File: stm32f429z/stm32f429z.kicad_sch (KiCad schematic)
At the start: 1 part, among them U1 STM32F429ZITx

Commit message: finished schematics and mostly finished the routing for the pcb
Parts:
- added C22: 100n, Capacitor_SMD:C_0603_1608Metric_Pad1.08x0.95mm_HandSolder, symbol Device:C
- added H1, H2, H3, H4: MountingHole, MountingHole:MountingHole_4.3mm_M4_Pad_Via, symbol Mechanical:MountingHole
- added SW1: Boot0, Button_Switch_SMD:SW_SPDT_CK-JS102011SAQN, symbol Switch:SW_SPDT
- added SW2: NRST, Button_Switch_SMD:SW_SPST_PTS645, symbol Switch:SW_Push
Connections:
- net +3.3V: now also U1.143 (PDR_ON), SW1.2 (B)
- net +3.3VA: now also U1.32 (VREF+)
- net CAN2_TX: no longer U1.114 (PD0)
- net GND: now also C22.2, SW1.3 (C), SW2.1
- net CAN SIlent Mode 1: now reaches U1.116 (PD2)
- net SPI3_CS  : now reaches U1.124 (PG9)
- net SYS_JTDO-SWO: now reaches U1.133 (PB3)
- net BOOT0: now reaches U1.138 (BOOT0)
- net BOOT0: now also SW1.1 (A)
- net NRST: now reaches U1.25 (NRST)
- net NRST: now also C22.1, SW2.2
- net CAN SIlent Mode 2: now reaches U1.76 (PB15)
- net USB_OTG_FS_DM renamed USB_OTG_FS_DP-
- net USB_OTG_FS_DP renamed USB_OTG_FS_DP+
- net USB_OTG_FS_ID: no longer names the net of U1.102 (PA10)
- net USB_OTG_FS_VBUS: no longer names the net of U1.101 (PA9)
- new net CAN1_RX: U1.114 (PD0)
- no-connect marks 0 -> 81
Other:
- removed sheet I2C
- removed sheet SPI
- removed sheet adc
- added sheet connectors (connectors.kicad_sch)

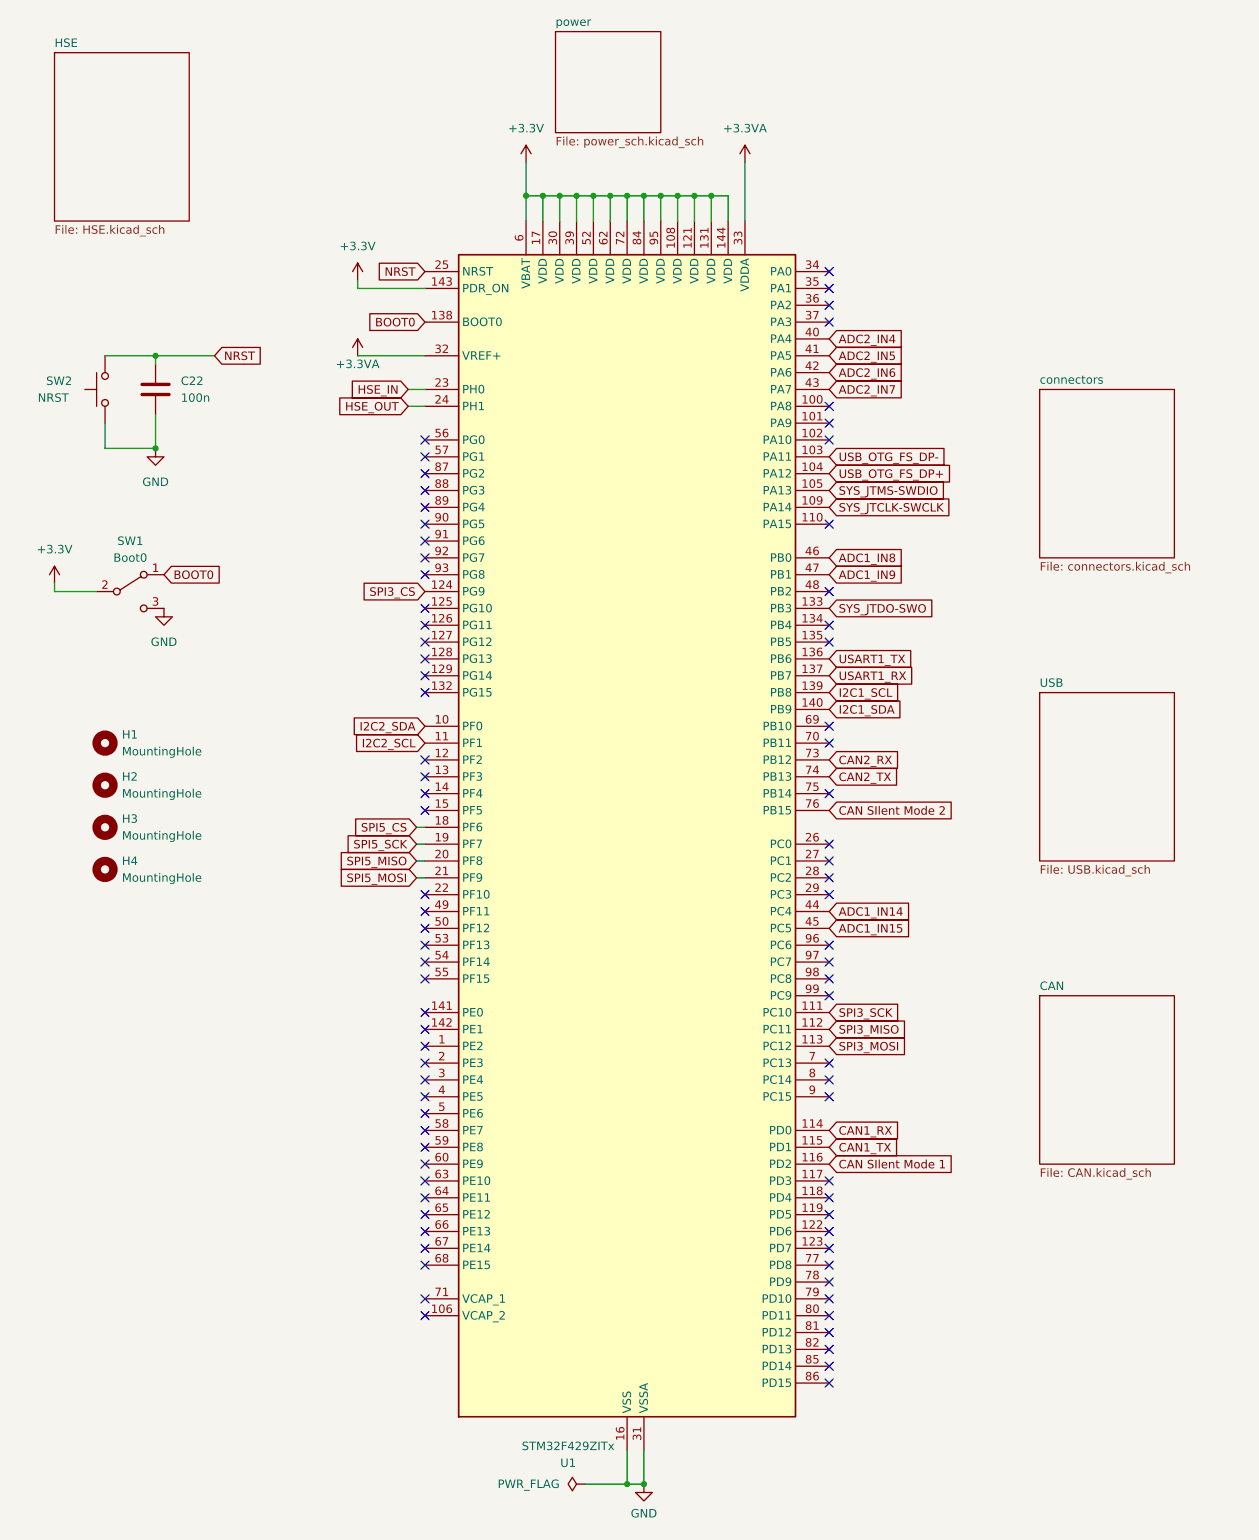
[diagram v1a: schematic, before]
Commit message: removed alot of the silk screen, changed oscillator foor print and added GPIOs
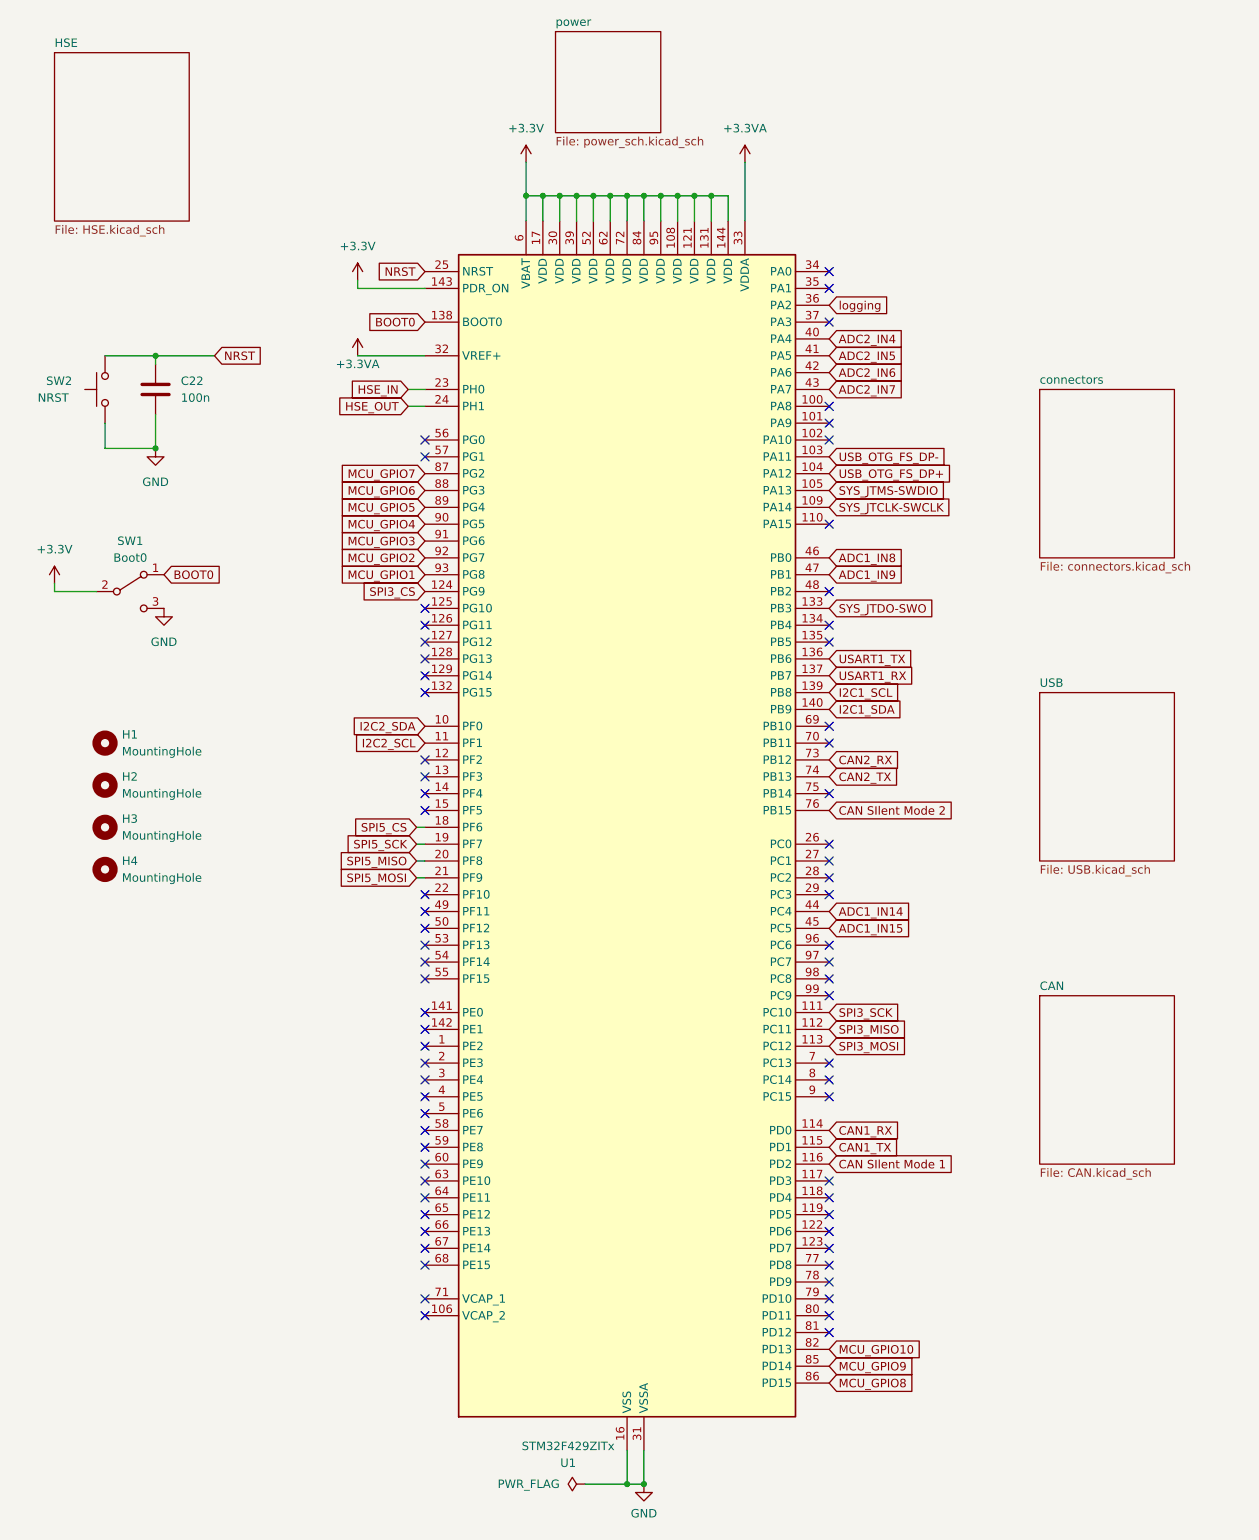
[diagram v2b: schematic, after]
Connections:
- net logging: now reaches U1.36 (PA2)
- net MCU_GPIO10: now reaches U1.82 (PD13)
- net MCU_GPIO9: now reaches U1.85 (PD14)
- net MCU_GPIO8: now reaches U1.86 (PD15)
- net MCU_GPIO7: now reaches U1.87 (PG2)
- net MCU_GPIO6: now reaches U1.88 (PG3)
- net MCU_GPIO5: now reaches U1.89 (PG4)
- net MCU_GPIO4: now reaches U1.90 (PG5)
- net MCU_GPIO3: now reaches U1.91 (PG6)
- net MCU_GPIO2: now reaches U1.92 (PG7)
- net MCU_GPIO1: now reaches U1.93 (PG8)
- no-connect marks 81 -> 70
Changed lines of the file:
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@@
   (no_connect (at 76.2 182.88))
   (no_connect (at 137.16 149.86))
-  (no_connect (at 137.16 220.98))
   (no_connect (at 76.2 114.3))
   (no_connect (at 137.16 195.58))
@@
   (no_connect (at 76.2 154.94))
   (no_connect (at 76.2 167.64))
-  (no_connect (at 137.16 218.44))
   (no_connect (at 76.2 175.26))
   (no_connect (at 137.16 63.5))
@@
   (no_connect (at 137.16 200.66))
   (no_connect (at 76.2 203.2))
-  (no_connect (at 137.16 223.52))
   (no_connect (at 137.16 111.76))
   (no_connect (at 137.16 104.14))
   (no_connect (at 76.2 193.04))
   (no_connect (at 137.16 157.48))
-  (no_connect (at 76.2 101.6))
   (no_connect (at 137.16 210.82))
-  (no_connect (at 76.2 91.44))
   (no_connect (at 76.2 157.48))
   (no_connect (at 137.16 76.2))
   (no_connect (at 137.16 142.24))
   (no_connect (at 76.2 172.72))
-  (no_connect (at 76.2 93.98))
   (no_connect (at 137.16 198.12))
   (no_connect (at 76.2 162.56))
-  (no_connect (at 76.2 99.06))
   (no_connect (at 76.2 190.5))
   (no_connect (at 76.2 132.08))
@@
   (no_connect (at 76.2 180.34))
   (no_connect (at 76.2 210.82))
-  (no_connect (at 76.2 96.52))
   (no_connect (at 137.16 160.02))
   (no_connect (at 76.2 149.86))
@@
   (no_connect (at 137.16 81.28))
   (no_connect (at 137.16 193.04))
-  (no_connect (at 76.2 86.36))
   (no_connect (at 137.16 93.98))
   (no_connect (at 76.2 200.66))
@@
   (no_connect (at 137.16 55.88))
   (no_connect (at 137.16 134.62))
-  (no_connect (at 137.16 60.96))
   (no_connect (at 76.2 83.82))
-  (no_connect (at 76.2 88.9))
   (no_connect (at 76.2 185.42))
   (no_connect (at 76.2 160.02))
@@
     )
   )
+  (global_label "MCU_GPIO9" (shape input) (at 137.16 220.98 0) (fields_autoplaced)
+    (effects (font (size 1.27 1.27)) (justify left))
+    (property "Intersheetrefs" "${INTERSHEET_REFS}" (at 150.8495 220.98 0)
+      (effects (font (size 1.27 1.27)) (justify left) hide)
+    )
+  )
   (global_label "I2C2_SDA" (shape input) (at 76.2 124.46 180) (fields_autoplaced)
     (effects (font (size 1.27 1.27)) (justify right))
@@
     )
   )
+  (global_label "MCU_GPIO6" (shape input) (at 76.2 88.9 180) (fields_autoplaced)
+    (effects (font (size 1.27 1.27)) (justify right))
+    (property "Intersheetrefs" "${INTERSHEET_REFS}" (at 62.5105 88.9 0)
+      (effects (font (size 1.27 1.27)) (justify right) hide)
+    )
+  )
+  (global_label "MCU_GPIO2" (shape input) (at 76.2 99.06 180) (fields_autoplaced)
+    (effects (font (size 1.27 1.27)) (justify right))
+    (property "Intersheetrefs" "${INTERSHEET_REFS}" (at 62.5105 99.06 0)
+      (effects (font (size 1.27 1.27)) (justify right) hide)
+    )
+  )
   (global_label "USART1_TX" (shape input) (at 137.16 114.3 0) (fields_autoplaced)
     (effects (font (size 1.27 1.27)) (justify left))
@@
     )
   )
+  (global_label "MCU_GPIO4" (shape input) (at 76.2 93.98 180) (fields_autoplaced)
+    (effects (font (size 1.27 1.27)) (justify right))
+    (property "Intersheetrefs" "${INTERSHEET_REFS}" (at 62.5105 93.98 0)
+      (effects (font (size 1.27 1.27)) (justify right) hide)
+    )
+  )
   (global_label "CAN1_TX" (shape input) (at 137.16 187.96 0) (fields_autoplaced)
     (effects (font (size 1.27 1.27)) (justify left))
@@
     )
   )
+  (global_label "MCU_GPIO5" (shape input) (at 76.2 91.44 180) (fields_autoplaced)
+    (effects (font (size 1.27 1.27)) (justify right))
+    (property "Intersheetrefs" "${INTERSHEET_REFS}" (at 62.5105 91.44 0)
+      (effects (font (size 1.27 1.27)) (justify right) hide)
+    )
+  )
   (global_label "ADC1_IN9" (shape input) (at 137.16 101.6 0) (fields_autoplaced)
     (effects (font (size 1.27 1.27)) (justify left))
@@
     )
   )
+  (global_label "MCU_GPIO3" (shape input) (at 76.2 96.52 180) (fields_autoplaced)
+    (effects (font (size 1.27 1.27)) (justify right))
+    (property "Intersheetrefs" "${INTERSHEET_REFS}" (at 62.5105 96.52 0)
+      (effects (font (size 1.27 1.27)) (justify right) hide)
+    )
+  )
+  (global_label "MCU_GPIO8" (shape input) (at 137.16 223.52 0) (fields_autoplaced)
+    (effects (font (size 1.27 1.27)) (justify left))
+    (property "Intersheetrefs" "${INTERSHEET_REFS}" (at 150.8495 223.52 0)
+      (effects (font (size 1.27 1.27)) (justify left) hide)
+    )
+  )
   (global_label "SPI3_MISO" (shape input) (at 137.16 170.18 0) (fields_autoplaced)
     (effects (font (size 1.27 1.27)) (justify left))
@@
     )
   )
+  (global_label "MCU_GPIO7" (shape input) (at 76.2 86.36 180) (fields_autoplaced)
+    (effects (font (size 1.27 1.27)) (justify right))
+    (property "Intersheetrefs" "${INTERSHEET_REFS}" (at 62.5105 86.36 0)
+      (effects (font (size 1.27 1.27)) (justify right) hide)
+    )
+  )
   (global_label "SYS_JTCLK-SWCLK" (shape input) (at 137.16 91.44 0) (fields_autoplaced)
     (effects (font (size 1.27 1.27)) (justify left))
@@
     )
   )
+  (global_label "MCU_GPIO1" (shape input) (at 76.2 101.6 180) (fields_autoplaced)
+    (effects (font (size 1.27 1.27)) (justify right))
+    (property "Intersheetrefs" "${INTERSHEET_REFS}" (at 62.5105 101.6 0)
+      (effects (font (size 1.27 1.27)) (justify right) hide)
+    )
+  )
   (global_label "ADC1_IN8" (shape input) (at 137.16 99.06 0) (fields_autoplaced)
     (effects (font (size 1.27 1.27)) (justify left))
@@
       (effects (font (size 1.27 1.27)) (justify left) hide)
     )
+  )
+  (global_label "logging" (shape input) (at 137.16 60.96 0) (fields_autoplaced)
+    (effects (font (size 1.27 1.27)) (justify left))
+    (property "Intersheetrefs" "${INTERSHEET_REFS}" (at 147.1602 60.96 0)
+      (effects (font (size 1.27 1.27)) (justify left) hide)
+    )
+  )
+  (global_label "MCU_GPIO10" (shape input) (at 137.16 218.44 0) (fields_autoplaced)
+    (effects (font (size 1.27 1.27)) (justify left))
+    (property "Intersheetrefs" "${INTERSHEET_REFS}" (at 152.059 218.44 0)
+      (effects (font (size 1.27 1.27)) (justify left) hide)
+    )
